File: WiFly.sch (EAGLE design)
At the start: 33 parts

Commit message: I honestly forgot what I updated
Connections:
- removed net N$5: U$2.GND2
- net GND: now also U$2.GND2
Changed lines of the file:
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@@
 <attribute name="VALUE" x="139.7" y="55.88" size="1.778" layer="96" rot="R90"/>
 </instance>
-<instance part="GND4" gate="1" x="198.12" y="66.04" smashed="yes">
-<attribute name="VALUE" x="195.58" y="63.5" size="1.778" layer="96"/>
+<instance part="GND4" gate="1" x="195.58" y="66.04" smashed="yes">
+<attribute name="VALUE" x="193.04" y="63.5" size="1.778" layer="96"/>
 </instance>
 <instance part="GND5" gate="1" x="190.5" y="45.72" smashed="yes">
@@
 <pinref part="GND14" gate="1" pin="GND"/>
 <wire x1="254" y1="40.64" x2="251.46" y2="40.64" width="0.1524" layer="91"/>
+</segment>
+<segment>
+<pinref part="GND4" gate="1" pin="GND"/>
+<wire x1="190.5" y1="68.58" x2="195.58" y2="68.58" width="0.1524" layer="91"/>
+<pinref part="U$2" gate="G$1" pin="GND2"/>
 </segment>
 </net>
@@
 <junction x="134.62" y="63.5"/>
 <label x="134.62" y="63.5" size="1.778" layer="95" xref="yes"/>
-</segment>
-</net>
-<net name="N$5" class="0">
-<segment>
-<pinref part="GND4" gate="1" pin="GND"/>
-<wire x1="190.5" y1="68.58" x2="198.12" y2="68.58" width="0.1524" layer="91"/>
-<pinref part="U$2" gate="G$1" pin="GND2"/>
 </segment>
 </net>
@@
 </sheet>
 </sheets>
-<errors>
-</errors>
 </schematic>
 </drawing>

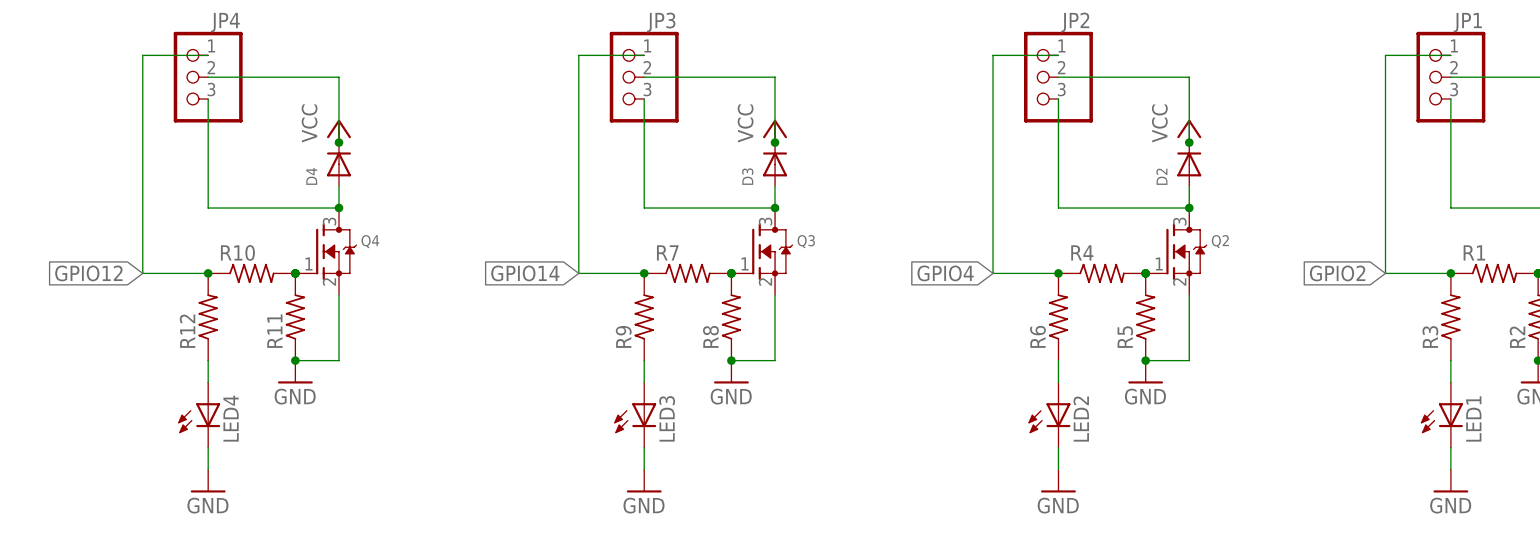
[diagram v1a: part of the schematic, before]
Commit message: Flipped ESP32CAM for physical layout, reworking other layouts
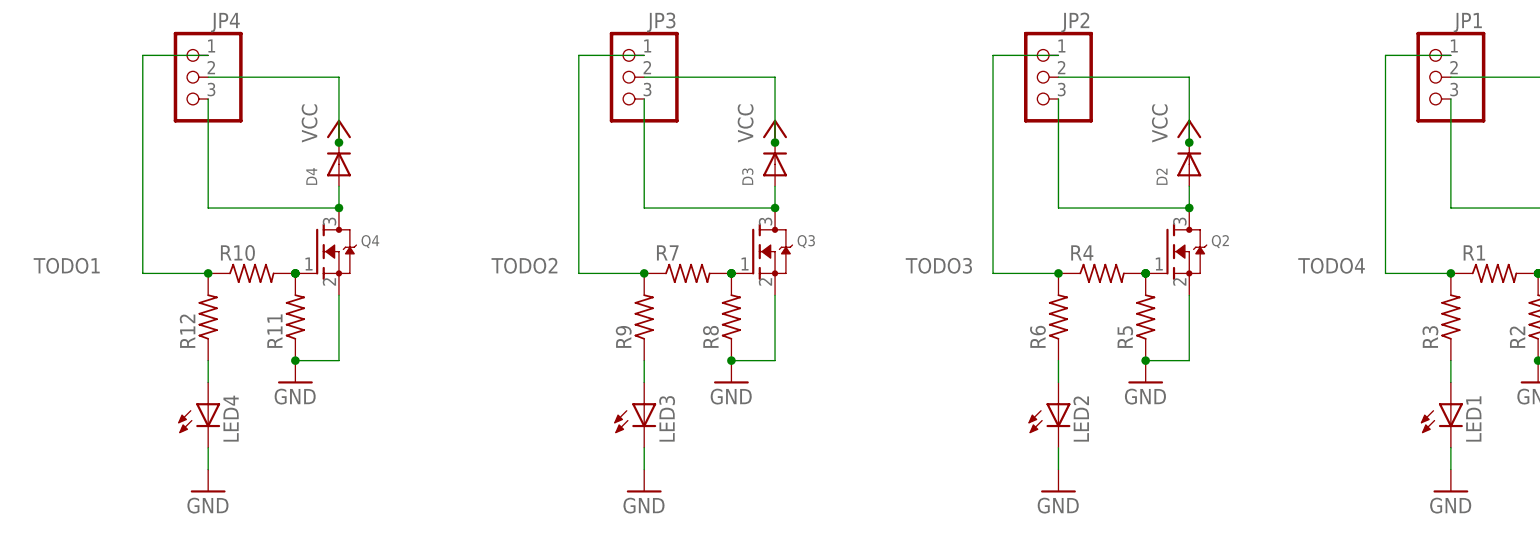
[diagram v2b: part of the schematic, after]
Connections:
- new net TODO1: JP4.1, R10.1, R12.2
- new net TODO2: JP3.1, R7.1, R9.2
- new net TODO3: JP2.1, R4.1, R6.2
- new net TODO4: JP1.1, R1.1, R3.2
- net GPIO12: no longer JP4.1, R10.1, R12.2
- net GPIO14: no longer JP3.1, R7.1, R9.2
- net GPIO2: no longer JP1.1, R1.1, R3.2
- net GPIO4: no longer JP2.1, R4.1, R6.2
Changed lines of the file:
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@@
 <label x="152.4" y="58.42" size="1.778" layer="95" rot="R180" xref="yes"/>
 </segment>
+</net>
+<net name="GPIO4" class="0">
+<segment>
+<pinref part="U$2" gate="G$1" pin="GPIO4"/>
+<junction x="152.4" y="48.26"/>
+<label x="152.4" y="48.26" size="1.778" layer="95" rot="R180" xref="yes"/>
+</segment>
+</net>
+<net name="GPIO2" class="0">
+<segment>
+<pinref part="U$2" gate="G$1" pin="GPIO2"/>
+<junction x="152.4" y="53.34"/>
+<label x="152.4" y="53.34" size="1.778" layer="95" rot="R180" xref="yes"/>
+</segment>
+</net>
+<net name="GPIO12" class="0">
+<segment>
+<pinref part="U$2" gate="G$1" pin="GPIO12"/>
+<junction x="152.4" y="73.66"/>
+<label x="152.4" y="73.66" size="1.778" layer="95" rot="R180" xref="yes"/>
+</segment>
+</net>
+<net name="TODO1" class="0">
+<segment>
+<pinref part="JP4" gate="A" pin="1"/>
+<wire x1="104.14" y1="25.4" x2="96.52" y2="25.4" width="0.1524" layer="91"/>
+<wire x1="96.52" y1="25.4" x2="96.52" y2="0" width="0.1524" layer="91"/>
+<pinref part="R10" gate="G$1" pin="1"/>
+<wire x1="96.52" y1="0" x2="104.14" y2="0" width="0.1524" layer="91"/>
+<pinref part="R12" gate="G$1" pin="2"/>
+<junction x="104.14" y="0"/>
+<label x="83.82" y="0" size="1.778" layer="95"/>
+</segment>
+</net>
+<net name="TODO2" class="0">
 <segment>
 <pinref part="JP3" gate="A" pin="1"/>
@@
 <pinref part="R9" gate="G$1" pin="2"/>
 <junction x="154.94" y="0"/>
-<label x="147.32" y="0" size="1.778" layer="95" rot="R180" xref="yes"/>
+<label x="137.16" y="0" size="1.778" layer="95"/>
 </segment>
 </net>
-<net name="GPIO4" class="0">
-<segment>
-<pinref part="U$2" gate="G$1" pin="GPIO4"/>
-<junction x="152.4" y="48.26"/>
-<label x="152.4" y="48.26" size="1.778" layer="95" rot="R180" xref="yes"/>
-</segment>
+<net name="TODO3" class="0">
 <segment>
 <pinref part="JP2" gate="A" pin="1"/>
@@
 <pinref part="R6" gate="G$1" pin="2"/>
 <junction x="203.2" y="0"/>
-<label x="195.58" y="0" size="1.778" layer="95" rot="R180" xref="yes"/>
+<label x="185.42" y="0" size="1.778" layer="95"/>
 </segment>
 </net>
-<net name="GPIO2" class="0">
-<segment>
-<pinref part="U$2" gate="G$1" pin="GPIO2"/>
-<junction x="152.4" y="53.34"/>
-<label x="152.4" y="53.34" size="1.778" layer="95" rot="R180" xref="yes"/>
-</segment>
+<net name="TODO4" class="0">
 <segment>
 <pinref part="JP1" gate="A" pin="1"/>
@@
 <pinref part="R3" gate="G$1" pin="2"/>
 <junction x="248.92" y="0"/>
-<label x="241.3" y="0" size="1.778" layer="95" rot="R180" xref="yes"/>
+<label x="231.14" y="0" size="1.778" layer="95"/>
 </segment>
 </net>
-<net name="GPIO12" class="0">
-<segment>
-<pinref part="U$2" gate="G$1" pin="GPIO12"/>
-<junction x="152.4" y="73.66"/>
-<label x="152.4" y="73.66" size="1.778" layer="95" rot="R180" xref="yes"/>
-</segment>
-<segment>
-<pinref part="JP4" gate="A" pin="1"/>
-<wire x1="104.14" y1="25.4" x2="96.52" y2="25.4" width="0.1524" layer="91"/>
-<wire x1="96.52" y1="25.4" x2="96.52" y2="0" width="0.1524" layer="91"/>
-<pinref part="R10" gate="G$1" pin="1"/>
-<wire x1="96.52" y1="0" x2="104.14" y2="0" width="0.1524" layer="91"/>
-<pinref part="R12" gate="G$1" pin="2"/>
-<junction x="104.14" y="0"/>
-<label x="96.52" y="0" size="1.778" layer="95" rot="R180" xref="yes"/>
-</segment>
-</net>

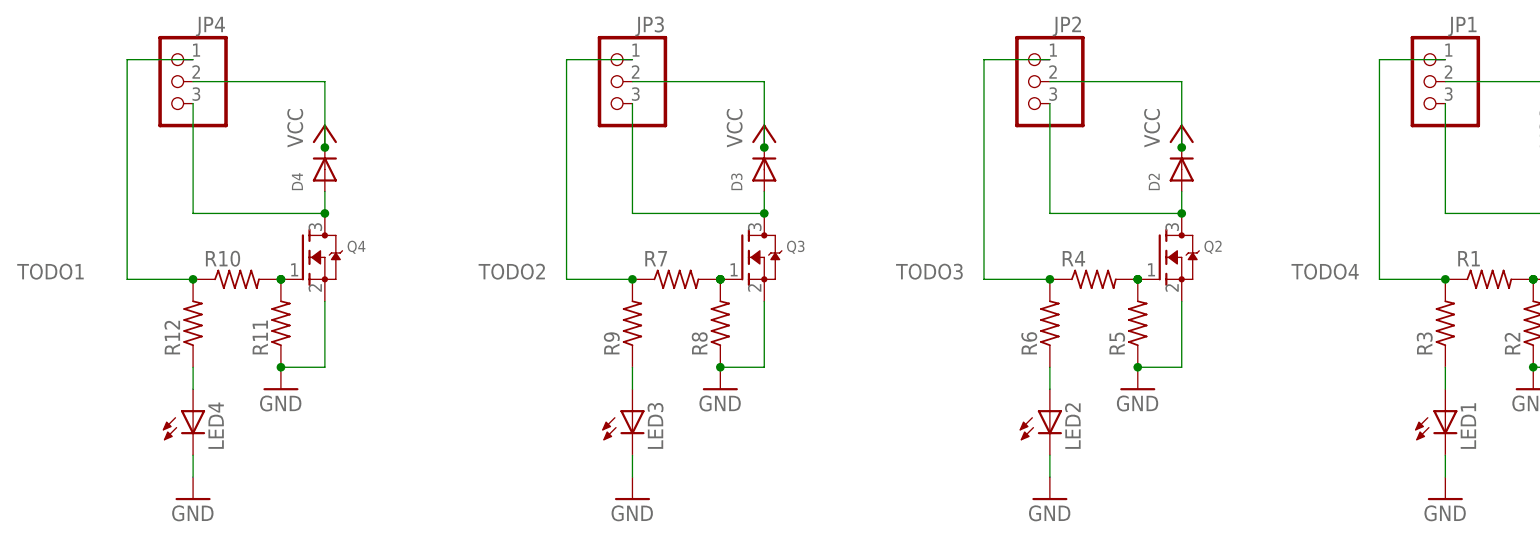
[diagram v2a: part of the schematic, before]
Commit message: Routed remaining wires and polygon pour, no errors ERC detected
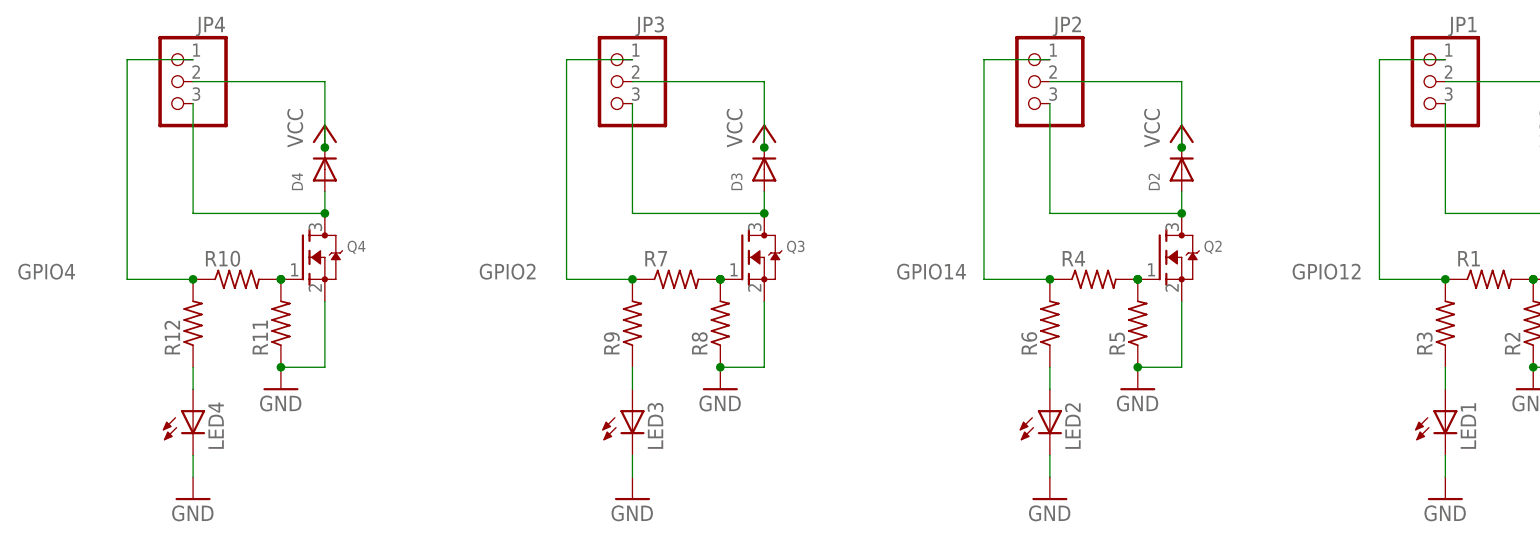
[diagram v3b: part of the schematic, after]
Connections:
- removed net TODO1: JP4.1, R10.1, R12.2
- removed net TODO2: JP3.1, R7.1, R9.2
- removed net TODO3: JP2.1, R4.1, R6.2
- removed net TODO4: JP1.1, R1.1, R3.2
- net GPIO12: now also JP1.1, R1.1, R3.2
- net GPIO14: now also JP2.1, R4.1, R6.2
- net GPIO2: now also JP3.1, R7.1, R9.2
- net GPIO4: now also JP4.1, R10.1, R12.2
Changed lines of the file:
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@@
 <label x="152.4" y="58.42" size="1.778" layer="95" rot="R180" xref="yes"/>
+</segment>
+<segment>
+<pinref part="JP2" gate="A" pin="1"/>
+<wire x1="203.2" y1="25.4" x2="195.58" y2="25.4" width="0.1524" layer="91"/>
+<wire x1="195.58" y1="25.4" x2="195.58" y2="0" width="0.1524" layer="91"/>
+<pinref part="R4" gate="G$1" pin="1"/>
+<wire x1="195.58" y1="0" x2="203.2" y2="0" width="0.1524" layer="91"/>
+<pinref part="R6" gate="G$1" pin="2"/>
+<junction x="203.2" y="0"/>
+<label x="185.42" y="0" size="1.778" layer="95"/>
 </segment>
 </net>
@@
 <label x="152.4" y="48.26" size="1.778" layer="95" rot="R180" xref="yes"/>
 </segment>
+<segment>
+<pinref part="JP4" gate="A" pin="1"/>
+<wire x1="104.14" y1="25.4" x2="96.52" y2="25.4" width="0.1524" layer="91"/>
+<wire x1="96.52" y1="25.4" x2="96.52" y2="0" width="0.1524" layer="91"/>
+<pinref part="R10" gate="G$1" pin="1"/>
+<wire x1="96.52" y1="0" x2="104.14" y2="0" width="0.0889" layer="91"/>
+<pinref part="R12" gate="G$1" pin="2"/>
+<junction x="104.14" y="0"/>
+<label x="83.82" y="0" size="1.778" layer="95"/>
+</segment>
 </net>
 <net name="GPIO2" class="0">
@@
 <label x="152.4" y="53.34" size="1.778" layer="95" rot="R180" xref="yes"/>
 </segment>
-</net>
-<net name="GPIO12" class="0">
-<segment>
-<pinref part="U$2" gate="G$1" pin="GPIO12"/>
-<junction x="152.4" y="73.66"/>
-<label x="152.4" y="73.66" size="1.778" layer="95" rot="R180" xref="yes"/>
-</segment>
-</net>
-<net name="TODO1" class="0">
-<segment>
-<pinref part="JP4" gate="A" pin="1"/>
-<wire x1="104.14" y1="25.4" x2="96.52" y2="25.4" width="0.1524" layer="91"/>
-<wire x1="96.52" y1="25.4" x2="96.52" y2="0" width="0.1524" layer="91"/>
-<pinref part="R10" gate="G$1" pin="1"/>
-<wire x1="96.52" y1="0" x2="104.14" y2="0" width="0.1524" layer="91"/>
-<pinref part="R12" gate="G$1" pin="2"/>
-<junction x="104.14" y="0"/>
-<label x="83.82" y="0" size="1.778" layer="95"/>
-</segment>
-</net>
-<net name="TODO2" class="0">
 <segment>
 <pinref part="JP3" gate="A" pin="1"/>
@@
 </segment>
 </net>
-<net name="TODO3" class="0">
+<net name="GPIO12" class="0">
 <segment>
-<pinref part="JP2" gate="A" pin="1"/>
-<wire x1="203.2" y1="25.4" x2="195.58" y2="25.4" width="0.1524" layer="91"/>
-<wire x1="195.58" y1="25.4" x2="195.58" y2="0" width="0.1524" layer="91"/>
-<pinref part="R4" gate="G$1" pin="1"/>
-<wire x1="195.58" y1="0" x2="203.2" y2="0" width="0.1524" layer="91"/>
-<pinref part="R6" gate="G$1" pin="2"/>
-<junction x="203.2" y="0"/>
-<label x="185.42" y="0" size="1.778" layer="95"/>
+<pinref part="U$2" gate="G$1" pin="GPIO12"/>
+<junction x="152.4" y="73.66"/>
+<label x="152.4" y="73.66" size="1.778" layer="95" rot="R180" xref="yes"/>
 </segment>
-</net>
-<net name="TODO4" class="0">
 <segment>
 <pinref part="JP1" gate="A" pin="1"/>

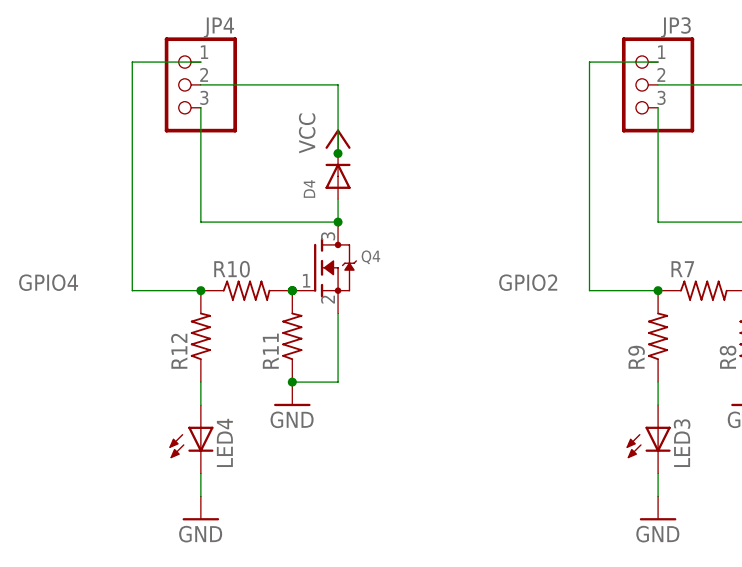
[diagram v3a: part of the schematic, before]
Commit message: Fix ESP32 layout and slide location down
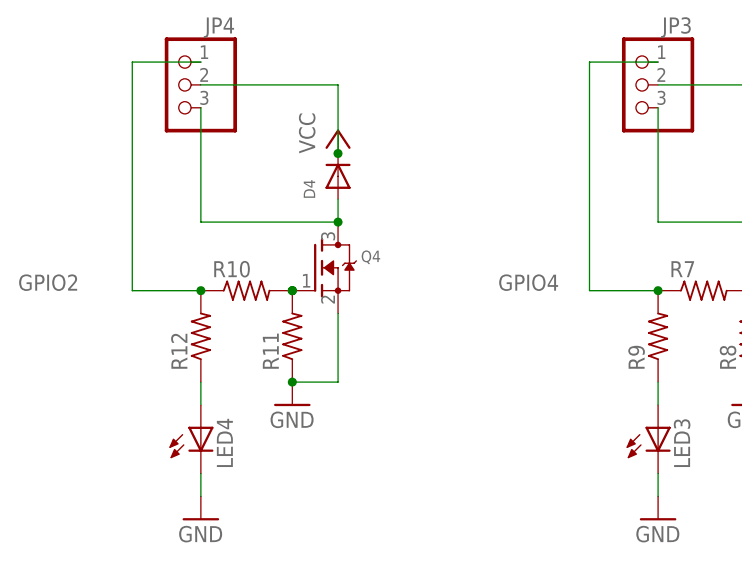
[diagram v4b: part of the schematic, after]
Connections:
- net GPIO2: now also JP4.1, R10.1, R12.2; no longer JP3.1, R7.1, R9.2
- net GPIO4: now also JP3.1, R7.1, R9.2; no longer JP4.1, R10.1, R12.2
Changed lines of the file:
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@@
+</segment>
+<segment>
+<pinref part="JP3" gate="A" pin="1"/>
+<wire x1="154.94" y1="25.4" x2="147.32" y2="25.4" width="0.1524" layer="91"/>
+<wire x1="147.32" y1="25.4" x2="147.32" y2="0" width="0.1524" layer="91"/>
+<pinref part="R7" gate="G$1" pin="1"/>
+<wire x1="147.32" y1="0" x2="154.94" y2="0" width="0.1524" layer="91"/>
+<pinref part="R9" gate="G$1" pin="2"/>
+<junction x="154.94" y="0"/>
+<label x="137.16" y="0" size="1.778" layer="95"/>
+</segment>
+</net>
+<net name="GPIO2" class="0">
+<segment>
+<pinref part="U$2" gate="G$1" pin="GPIO2"/>
+<junction x="152.4" y="53.34"/>
+<label x="152.4" y="53.34" size="1.778" layer="95" rot="R180" xref="yes"/>
 </segment>
 <segment>
@@
 </segment>
 </net>
-<net name="GPIO2" class="0">
-<segment>
-<pinref part="U$2" gate="G$1" pin="GPIO2"/>
-<junction x="152.4" y="53.34"/>
-<label x="152.4" y="53.34" size="1.778" layer="95" rot="R180" xref="yes"/>
-</segment>
-<segment>
-<pinref part="JP3" gate="A" pin="1"/>
-<wire x1="154.94" y1="25.4" x2="147.32" y2="25.4" width="0.1524" layer="91"/>
-<wire x1="147.32" y1="25.4" x2="147.32" y2="0" width="0.1524" layer="91"/>
-<pinref part="R7" gate="G$1" pin="1"/>
-<wire x1="147.32" y1="0" x2="154.94" y2="0" width="0.1524" layer="91"/>
-<pinref part="R9" gate="G$1" pin="2"/>
-<junction x="154.94" y="0"/>
-<label x="137.16" y="0" size="1.778" layer="95"/>
-</segment>
-</net>
